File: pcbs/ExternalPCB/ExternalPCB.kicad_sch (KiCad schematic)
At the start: 31 parts, among them J1 Bat +, J2 Bat -, J3 Conn_01x04_Pin, J4 Conn_01x04_Pin, J5 Conn_01x02_Pin, J6 Conn_01x03_Pin, J6 Conn_01x04_Pin, J7 Conn_01x03_Pin, J8 Conn_01x04_Pin, J8 Conn_01x05_Pin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

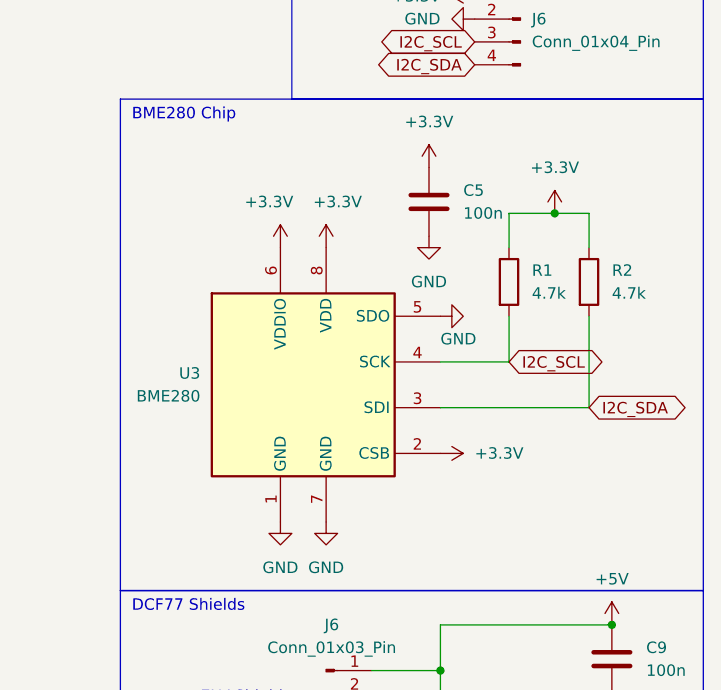
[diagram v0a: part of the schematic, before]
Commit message: DNP BME280 IC
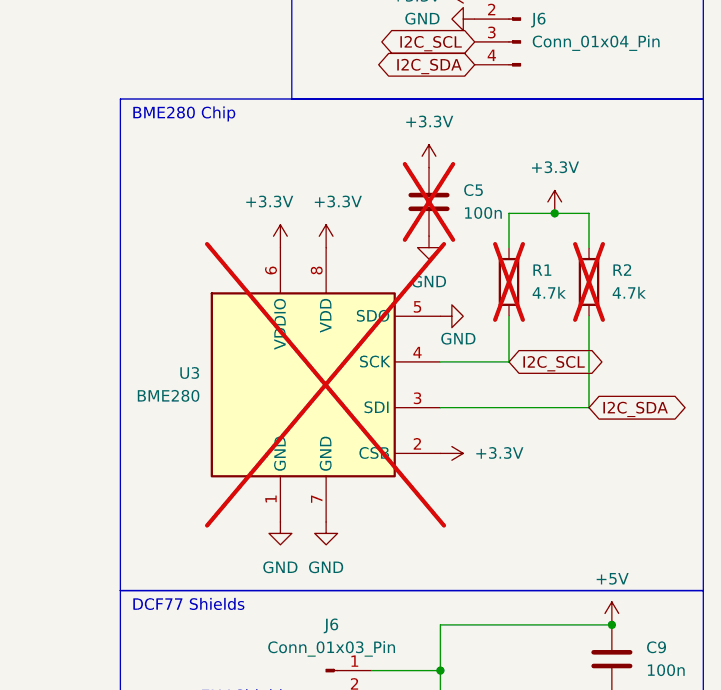
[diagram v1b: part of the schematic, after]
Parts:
- C5, R1, R2, U3: now not fitted
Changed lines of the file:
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@@
   )
   (symbol (lib_id "Device:C") (at 254 46.99 0) (unit 1)
-    (in_bom yes) (on_board yes) (dnp no) (fields_autoplaced)
+    (in_bom yes) (on_board yes) (dnp yes) (fields_autoplaced)
     (property "Reference" "C5" (at 257.81 45.72 0)
       (effects (font (size 1.27 1.27)) (justify left))
@@
   )
   (symbol (lib_id "Sensor:BME280") (at 240.03 67.31 0) (unit 1)
-    (in_bom yes) (on_board yes) (dnp no) (fields_autoplaced)
+    (in_bom yes) (on_board yes) (dnp yes) (fields_autoplaced)
     (property "Reference" "U3" (at 228.6 66.04 0)
       (effects (font (size 1.27 1.27)) (justify right))
@@
   )
   (symbol (lib_id "Device:R") (at 271.78 55.88 0) (unit 1)
-    (in_bom yes) (on_board yes) (dnp no)
+    (in_bom yes) (on_board yes) (dnp yes)
     (property "Reference" "R2" (at 274.32 54.61 0)
       (effects (font (size 1.27 1.27)) (justify left))
@@
   )
   (symbol (lib_id "Device:R") (at 262.89 55.88 0) (unit 1)
-    (in_bom yes) (on_board yes) (dnp no)
+    (in_bom yes) (on_board yes) (dnp yes)
     (property "Reference" "R1" (at 265.43 54.61 0)
       (effects (font (size 1.27 1.27)) (justify left))

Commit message: JLCPCB hatte ein paar Teile nicht...
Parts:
- removed L1, L2: EPL3015-472MLC, EPL3015:EPL3015472MLC, symbol EPL3015-472MLC:EPL3015-472MLC
- removed U2: TPS61221DCK, Package_TO_SOT_SMD:Texas_R-PDSO-G6, symbol Regulator_Switching:TPS61221DCK
- added L1, L2: LQH44PN4R7MJ0L, LQH44PN4R7MJ0L:LQH44PN100MJ0L, symbol LQH44PN4R7MJ0L:LQH44PN4R7MJ0L
- added PS1: TPS61097A-33DBVR, TPS61097A:SOT95P280X145-5N, symbol TPS61097A-33DBVR:TPS61097A-33DBVR
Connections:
- net +3.3V: now also PS1.4 (VOUT)
- net +BATT: now also L1.1, L2.1, PS1.1 (VIN), PS1.3 (EN)
- net -BATT: now also PS1.2 (GND)
- net at U1.5 (L): now also L1.2
- new net: L2.2, PS1.5 (L)
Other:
- moved on the sheet: C2, C4, C8
